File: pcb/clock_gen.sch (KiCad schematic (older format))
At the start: 0 parts

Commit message: schematic completed. Time for review
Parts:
- added C? (x2): 4.7u, symbol C
- added C? (x7): 0.47u, symbol C
- added FB? (x2): FILTER, symbol FILTER
- added U?: Si5338C, symbol Si5338C
- added U?: FOX924, symbol FOX924
- added U?: PL133-27, symbol PL133-27
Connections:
- net labels added: +3V3, CLK_GEN_IN, CLK_SCL, CLK_SDA, CLOCK_GEN_POWER, FPGA_CLK, GND, GTP_CLK_N, GTP_CLK_P, OSC_POWER, RF_CLK, RX_CLK, RX_CLK_FPGA, TX_CLK, TX_CLK_FPGA
- wire segments 0 -> 68

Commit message: Added part numbers and updated schematic
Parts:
- gave numbers to parts that had none: 14
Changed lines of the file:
@@
 $EndDescr
 $Comp
-L Si5338C U?
+L Si5338C U1003
 U 1 1 565F531B
 P 7600 2650
-F 0 "U?" H 7150 1750 60  0000 C CNN
+F 0 "U1003" H 7150 1750 60  0000 C CNN
 F 1 "Si5338C" H 7300 3550 60  0000 C CNN
 F 2 "" H 7400 2700 60  0000 C CNN
@@
 $EndComp
 $Comp
-L FOX924 U?
+L FOX924 U1001
 U 1 1 565F579F
 P 1900 1900
-F 0 "U?" H 1650 1550 60  0000 C CNN
+F 0 "U1001" H 1650 1550 60  0000 C CNN
 F 1 "FOX924" H 1750 2250 60  0000 C CNN
 F 2 "" H 1850 1800 60  0000 C CNN
@@
 $EndComp
 $Comp
-L PL133-27 U?
+L PL133-27 U1002
 U 1 1 565F5848
 P 3550 1850
-F 0 "U?" H 3350 1550 60  0000 C CNN
+F 0 "U1002" H 3350 1550 60  0000 C CNN
 F 1 "PL133-27" H 3550 2150 60  0000 C CNN
 F 2 "" H 3600 1700 60  0000 C CNN
@@
 $EndComp
 $Comp
-L GND #PWR?
+L GND #PWR1005
 U 1 1 565F599D
 P 3000 2300
-F 0 "#PWR?" H 3000 2050 50  0001 C CNN
+F 0 "#PWR1005" H 3000 2050 50  0001 C CNN
 F 1 "GND" H 3000 2150 50  0000 C CNN
 F 2 "" H 3000 2300 60  0000 C CNN
@@
 $EndComp
 $Comp
-L GND #PWR?
+L GND #PWR1001
 U 1 1 565F59BA
 P 1300 2300
-F 0 "#PWR?" H 1300 2050 50  0001 C CNN
+F 0 "#PWR1001" H 1300 2050 50  0001 C CNN
 F 1 "GND" H 1300 2150 50  0000 C CNN
 F 2 "" H 1300 2300 60  0000 C CNN
@@
 $EndComp
 $Comp
-L GND #PWR?
+L GND #PWR1009
 U 1 1 565F59F5
 P 6800 3500
-F 0 "#PWR?" H 6800 3250 50  0001 C CNN
+F 0 "#PWR1009" H 6800 3250 50  0001 C CNN
 F 1 "GND" H 6800 3350 50  0000 C CNN
 F 2 "" H 6800 3500 60  0000 C CNN
@@
 $EndComp
 $Comp
-L FILTER FB?
+L FILTER FB1002
 U 1 1 565F5A21
 P 2450 3700
-F 0 "FB?" H 2450 3850 50  0000 C CNN
+F 0 "FB1002" H 2450 3850 50  0000 C CNN
 F 1 "FILTER" H 2450 3600 50  0000 C CNN
 F 2 "" H 2450 3700 60  0000 C CNN
@@
 $EndComp
 $Comp
-L C C?
+L C C1002
 U 1 1 565F5A5C
 P 3000 3950
-F 0 "C?" H 3025 4050 50  0000 L CNN
+F 0 "C1002" H 3025 4050 50  0000 L CNN
 F 1 "4.7u" H 3025 3850 50  0000 L CNN
 F 2 "" H 3038 3800 30  0000 C CNN
@@
 $EndComp
 $Comp
-L C C?
+L C C1004
 U 1 1 565F5A91
 P 3300 3950
-F 0 "C?" H 3325 4050 50  0000 L CNN
+F 0 "C1004" H 3325 4050 50  0000 L CNN
 F 1 "0.47u" H 3325 3850 50  0000 L CNN
 F 2 "" H 3338 3800 30  0000 C CNN
@@
 $EndComp
 $Comp
-L C C?
+L C C1006
 U 1 1 565F5ABD
 P 3600 3950
-F 0 "C?" H 3625 4050 50  0000 L CNN
+F 0 "C1006" H 3625 4050 50  0000 L CNN
 F 1 "0.47u" H 3625 3850 50  0000 L CNN
 F 2 "" H 3638 3800 30  0000 C CNN
@@
 $EndComp
 $Comp
-L +3V3 #PWR?
+L +3V3 #PWR1003
 U 1 1 565F5B53
 P 2000 3600
-F 0 "#PWR?" H 2000 3450 50  0001 C CNN
+F 0 "#PWR1003" H 2000 3450 50  0001 C CNN
 F 1 "+3V3" H 2000 3740 50  0000 C CNN
 F 2 "" H 2000 3600 60  0000 C CNN
@@
 $EndComp
 $Comp
-L GND #PWR?
+L GND #PWR1006
 U 1 1 565F5C73
 P 3000 4300
-F 0 "#PWR?" H 3000 4050 50  0001 C CNN
+F 0 "#PWR1006" H 3000 4050 50  0001 C CNN
 F 1 "GND" H 3000 4150 50  0000 C CNN
 F 2 "" H 3000 4300 60  0000 C CNN
@@
 OSC_POWER
 $Comp
-L FILTER FB?
+L FILTER FB1001
 U 1 1 565F5D36
 P 2350 4800
-F 0 "FB?" H 2350 4950 50  0000 C CNN
+F 0 "FB1001" H 2350 4950 50  0000 C CNN
 F 1 "FILTER" H 2350 4700 50  0000 C CNN
 F 2 "" H 2350 4800 60  0000 C CNN
@@
 $EndComp
 $Comp
-L C C?
+L C C1001
 U 1 1 565F5D3C
 P 2900 5050
-F 0 "C?" H 2925 5150 50  0000 L CNN
+F 0 "C1001" H 2925 5150 50  0000 L CNN
 F 1 "4.7u" H 2925 4950 50  0000 L CNN
 F 2 "" H 2938 4900 30  0000 C CNN
@@
 $EndComp
 $Comp
-L C C?
+L C C1003
 U 1 1 565F5D42
 P 3200 5050
-F 0 "C?" H 3225 5150 50  0000 L CNN
+F 0 "C1003" H 3225 5150 50  0000 L CNN
 F 1 "0.47u" H 3225 4950 50  0000 L CNN
 F 2 "" H 3238 4900 30  0000 C CNN
@@
 $EndComp
 $Comp
-L C C?
+L C C1009
 U 1 1 565F5D48
 P 4300 5050
-F 0 "C?" H 4325 5150 50  0000 L CNN
+F 0 "C1009" H 4325 5150 50  0000 L CNN
 F 1 "0.47u" H 4325 4950 50  0000 L CNN
 F 2 "" H 4338 4900 30  0000 C CNN
@@
 $EndComp
 $Comp
-L +3V3 #PWR?
+L +3V3 #PWR1002
 U 1 1 565F5D4E
 P 1900 4700
-F 0 "#PWR?" H 1900 4550 50  0001 C CNN
+F 0 "#PWR1002" H 1900 4550 50  0001 C CNN
 F 1 "+3V3" H 1900 4840 50  0000 C CNN
 F 2 "" H 1900 4700 60  0000 C CNN
@@
 $EndComp
 $Comp
-L GND #PWR?
+L GND #PWR1004
 U 1 1 565F5D61
 P 2900 5400
-F 0 "#PWR?" H 2900 5150 50  0001 C CNN
+F 0 "#PWR1004" H 2900 5150 50  0001 C CNN
 F 1 "GND" H 2900 5250 50  0000 C CNN
 F 2 "" H 2900 5400 60  0000 C CNN
@@
 CLOCK_GEN_POWER
 $Comp
-L C C?
+L C C1005
 U 1 1 565F5DDA
 P 3500 5050
-F 0 "C?" H 3525 5150 50  0000 L CNN
+F 0 "C1005" H 3525 5150 50  0000 L CNN
 F 1 "0.47u" H 3525 4950 50  0000 L CNN
 F 2 "" H 3538 4900 30  0000 C CNN
@@
 $EndComp
 $Comp
-L C C?
+L C C1007
 U 1 1 565F5E43
 P 3800 5050
-F 0 "C?" H 3825 5150 50  0000 L CNN
+F 0 "C1007" H 3825 5150 50  0000 L CNN
 F 1 "0.47u" H 3825 4950 50  0000 L CNN
 F 2 "" H 3838 4900 30  0000 C CNN
@@
 $EndComp
 $Comp
-L C C?
+L C C1008
 U 1 1 565F607C
 P 4050 5050
-F 0 "C?" H 4075 5150 50  0000 L CNN
+F 0 "C1008" H 4075 5150 50  0000 L CNN
 F 1 "0.47u" H 4075 4950 50  0000 L CNN
 F 2 "" H 4088 4900 30  0000 C CNN
@@
 CLK_GEN_IN
 $Comp
-L GND #PWR?
+L GND #PWR1007
 U 1 1 565F65BD
 P 6500 2200
-F 0 "#PWR?" H 6500 1950 50  0001 C CNN
+F 0 "#PWR1007" H 6500 1950 50  0001 C CNN
 F 1 "GND" H 6500 2050 50  0000 C CNN
 F 2 "" H 6500 2200 60  0000 C CNN
@@
 CLK_GEN_IN
 $Comp
-L GND #PWR?
+L GND #PWR1008
 U 1 1 565F66BC
 P 6500 2600
-F 0 "#PWR?" H 6500 2350 50  0001 C CNN
+F 0 "#PWR1008" H 6500 2350 50  0001 C CNN
 F 1 "GND" H 6500 2450 50  0000 C CNN
 F 2 "" H 6500 2600 60  0000 C CNN

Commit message: mostly done with component placement
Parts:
- removed U1002: PL133-27, symbol PL133-27
- added U1002: NB3L553, wbraun_smd:DFN-8_2x2mm_Pitch0.5mm, symbol NB3L553
- C1001, C1002, C1003, C1004, C1005, C1006, C1007, C1008, C1009: footprint (none) -> wbraun_smd:C_0402
- FB1001, FB1002: footprint (none) -> wbraun_smd:L_0603
- U1001: footprint (none) -> wbraun_smd:OSCILLATOR_5.0X3.2
- U1003: footprint (none) -> wbraun_smd:QFN-24-1EP_4x4mm_Pitch0.5mm
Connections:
- wire segments 68 -> 69

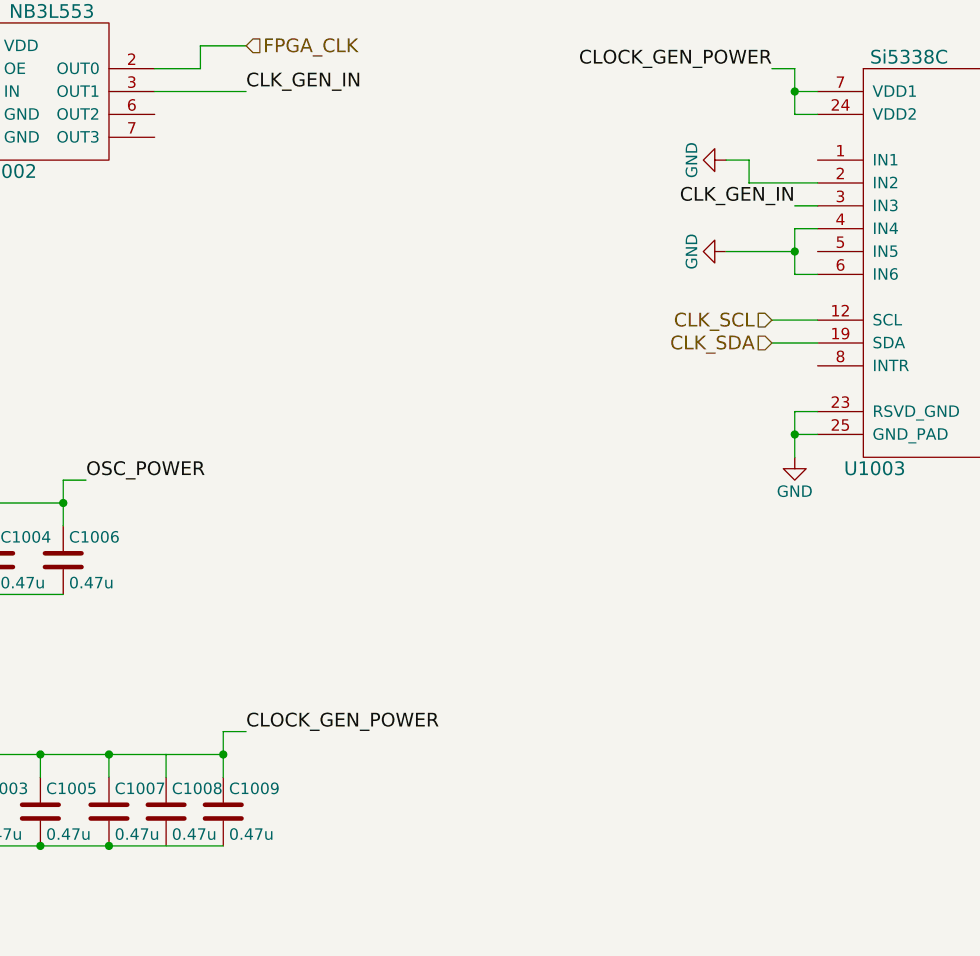
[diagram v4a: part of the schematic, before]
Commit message: Finished most of the routing, removed DDR-3
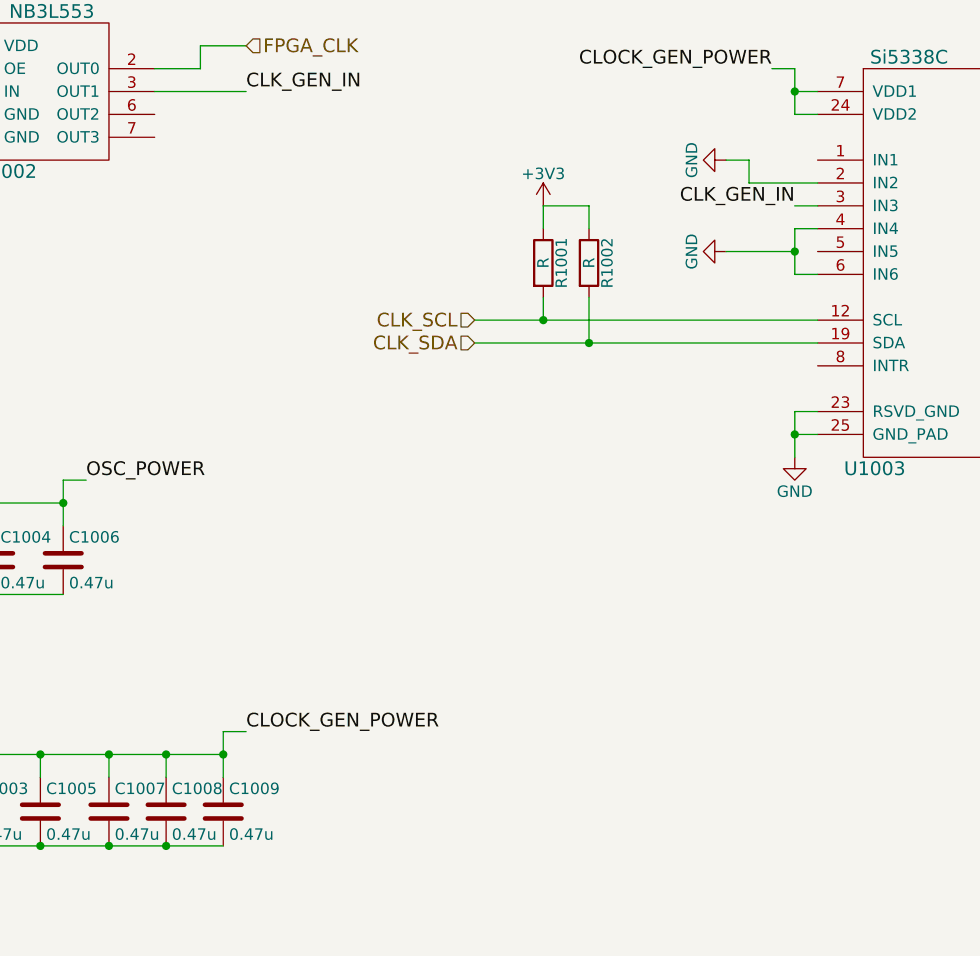
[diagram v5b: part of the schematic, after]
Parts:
- added R1001, R1002: R, wbraun_smd:R_0402, symbol R
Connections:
- net +3V3: now also R1001.1, R1002.1
- net CLK_SCL: now also R1001.2
- net CLK_SDA: now also R1002.2
- net CLOCK_GEN_POWER: now also C1008.1
- net GND: now also C1008.2
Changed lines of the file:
@@
 $Descr A4 11693 8268
 encoding utf-8
-Sheet 10 13
+Sheet 8 11
 Title ""
 Date ""
@@
 $EndComp
 $Comp
-L GND #PWR0144
+L GND #PWR0128
 U 1 1 565F599D
 P 3000 2300
-F 0 "#PWR0144" H 3000 2050 50  0001 C CNN
+F 0 "#PWR0128" H 3000 2050 50  0001 C CNN
 F 1 "GND" H 3000 2150 50  0000 C CNN
 F 2 "" H 3000 2300 60  0000 C CNN
@@
 $EndComp
 $Comp
-L GND #PWR0145
+L GND #PWR0129
 U 1 1 565F59BA
 P 1300 2300
-F 0 "#PWR0145" H 1300 2050 50  0001 C CNN
+F 0 "#PWR0129" H 1300 2050 50  0001 C CNN
 F 1 "GND" H 1300 2150 50  0000 C CNN
 F 2 "" H 1300 2300 60  0000 C CNN
@@
 $EndComp
 $Comp
-L GND #PWR0146
+L GND #PWR0130
 U 1 1 565F59F5
 P 6800 3500
-F 0 "#PWR0146" H 6800 3250 50  0001 C CNN
+F 0 "#PWR0130" H 6800 3250 50  0001 C CNN
 F 1 "GND" H 6800 3350 50  0000 C CNN
 F 2 "" H 6800 3500 60  0000 C CNN
@@
 $EndComp
 $Comp
-L +3V3 #PWR0147
+L +3V3 #PWR0131
 U 1 1 565F5B53
 P 2000 3600
-F 0 "#PWR0147" H 2000 3450 50  0001 C CNN
+F 0 "#PWR0131" H 2000 3450 50  0001 C CNN
 F 1 "+3V3" H 2000 3740 50  0000 C CNN
 F 2 "" H 2000 3600 60  0000 C CNN
@@
 $EndComp
 $Comp
-L GND #PWR0148
+L GND #PWR0132
 U 1 1 565F5C73
 P 3000 4300
-F 0 "#PWR0148" H 3000 4050 50  0001 C CNN
+F 0 "#PWR0132" H 3000 4050 50  0001 C CNN
 F 1 "GND" H 3000 4150 50  0000 C CNN
 F 2 "" H 3000 4300 60  0000 C CNN
@@
 $EndComp
 $Comp
-L +3V3 #PWR0149
+L +3V3 #PWR0133
 U 1 1 565F5D4E
 P 1900 4700
-F 0 "#PWR0149" H 1900 4550 50  0001 C CNN
+F 0 "#PWR0133" H 1900 4550 50  0001 C CNN
 F 1 "+3V3" H 1900 4840 50  0000 C CNN
 F 2 "" H 1900 4700 60  0000 C CNN
@@
 $EndComp
 $Comp
-L GND #PWR0150
+L GND #PWR0134
 U 1 1 565F5D61
 P 2900 5400
-F 0 "#PWR0150" H 2900 5150 50  0001 C CNN
+F 0 "#PWR0134" H 2900 5150 50  0001 C CNN
 F 1 "GND" H 2900 5250 50  0000 C CNN
 F 2 "" H 2900 5400 60  0000 C CNN
@@
 CLK_GEN_IN
 $Comp
-L GND #PWR0151
+L GND #PWR0135
 U 1 1 565F65BD
 P 6500 2200
-F 0 "#PWR0151" H 6500 1950 50  0001 C CNN
+F 0 "#PWR0135" H 6500 1950 50  0001 C CNN
 F 1 "GND" H 6500 2050 50  0000 C CNN
 F 2 "" H 6500 2200 60  0000 C CNN
@@
 CLK_GEN_IN
 $Comp
-L GND #PWR0152
+L GND #PWR0136
 U 1 1 565F66BC
 P 6500 2600
-F 0 "#PWR0152" H 6500 2350 50  0001 C CNN
+F 0 "#PWR0136" H 6500 2350 50  0001 C CNN
 F 1 "GND" H 6500 2450 50  0000 C CNN
 F 2 "" H 6500 2600 60  0000 C CNN
@@
 Text HLabel 8500 3300 2    60   Input ~ 0
 GTP_CLK_N
-Text HLabel 6700 2900 0    60   Input ~ 0
+Text HLabel 5400 2900 0    60   Input ~ 0
 CLK_SCL
-Text HLabel 6700 3000 0    60   Input ~ 0
+Text HLabel 5400 3000 0    60   Input ~ 0
 CLK_SDA
 Text HLabel 8500 2500 2    60   Input ~ 0
@@
 	8300 3300 8500 3300
 Wire Wire Line
-	6900 2900 6700 2900
-Wire Wire Line
-	6900 3000 6700 3000
+	5400 2900 6900 2900
+Wire Wire Line
+	5400 3000 6900 3000
 Wire Wire Line
 	3000 2000 3000 2300
@@
 Wire Wire Line
 	4400 1900 4000 1900
+$Comp
+L R R1001
+U 1 1 56672DC6
+P 5700 2650
+F 0 "R1001" V 5780 2650 50  0000 C CNN
+F 1 "R" V 5700 2650 50  0000 C CNN
+F 2 "wbraun_smd:R_0402" V 5630 2650 50  0001 C CNN
+F 3 "" H 5700 2650 50  0000 C CNN
+	1    5700 2650
+	1    0    0    -1
+$EndComp
+$Comp
+L R R1002
+U 1 1 56672EA0
+P 5900 2650
+F 0 "R1002" V 5980 2650 50  0000 C CNN
+F 1 "R" V 5900 2650 50  0000 C CNN
+F 2 "wbraun_smd:R_0402" V 5830 2650 50  0001 C CNN
+F 3 "" H 5900 2650 50  0000 C CNN
+	1    5900 2650
+	1    0    0    -1
+$EndComp
+Wire Wire Line
+	5700 2800 5700 2900
+Connection ~ 5700 2900
+Wire Wire Line
+	5900 2800 5900 3000
+Connection ~ 5900 3000
+$Comp
+L +3V3 #PWR0137
+U 1 1 5667326B
+P 5700 2400
+F 0 "#PWR0137" H 5700 2250 50  0001 C CNN
+F 1 "+3V3" H 5700 2540 50  0000 C CNN
+F 2 "" H 5700 2400 60  0000 C CNN
+F 3 "" H 5700 2400 60  0000 C CNN
+	1    5700 2400
+	1    0    0    -1
+$EndComp
+Wire Wire Line
+	5900 2500 5900 2400
+Wire Wire Line
+	5900 2400 5700 2400
+Wire Wire Line
+	5700 2400 5700 2500
+Connection ~ 4050 4800
+Connection ~ 4050 5200
 $EndSCHEMATC

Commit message: Pending final check
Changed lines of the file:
@@
 $EndComp
 $Comp
-L GND #PWR0128
+L GND #PWR0129
 U 1 1 565F599D
 P 3000 2300
-F 0 "#PWR0128" H 3000 2050 50  0001 C CNN
+F 0 "#PWR0129" H 3000 2050 50  0001 C CNN
 F 1 "GND" H 3000 2150 50  0000 C CNN
 F 2 "" H 3000 2300 60  0000 C CNN
@@
 $EndComp
 $Comp
-L GND #PWR0129
+L GND #PWR0130
 U 1 1 565F59BA
 P 1300 2300
-F 0 "#PWR0129" H 1300 2050 50  0001 C CNN
+F 0 "#PWR0130" H 1300 2050 50  0001 C CNN
 F 1 "GND" H 1300 2150 50  0000 C CNN
 F 2 "" H 1300 2300 60  0000 C CNN
@@
 $EndComp
 $Comp
-L GND #PWR0130
+L GND #PWR0131
 U 1 1 565F59F5
 P 6800 3500
-F 0 "#PWR0130" H 6800 3250 50  0001 C CNN
+F 0 "#PWR0131" H 6800 3250 50  0001 C CNN
 F 1 "GND" H 6800 3350 50  0000 C CNN
 F 2 "" H 6800 3500 60  0000 C CNN
@@
 $EndComp
 $Comp
-L +3V3 #PWR0131
+L +3V3 #PWR0132
 U 1 1 565F5B53
 P 2000 3600
-F 0 "#PWR0131" H 2000 3450 50  0001 C CNN
+F 0 "#PWR0132" H 2000 3450 50  0001 C CNN
 F 1 "+3V3" H 2000 3740 50  0000 C CNN
 F 2 "" H 2000 3600 60  0000 C CNN
@@
 $EndComp
 $Comp
-L GND #PWR0132
+L GND #PWR0133
 U 1 1 565F5C73
 P 3000 4300
-F 0 "#PWR0132" H 3000 4050 50  0001 C CNN
+F 0 "#PWR0133" H 3000 4050 50  0001 C CNN
 F 1 "GND" H 3000 4150 50  0000 C CNN
 F 2 "" H 3000 4300 60  0000 C CNN
@@
 $EndComp
 $Comp
-L +3V3 #PWR0133
+L +3V3 #PWR0134
 U 1 1 565F5D4E
 P 1900 4700
-F 0 "#PWR0133" H 1900 4550 50  0001 C CNN
+F 0 "#PWR0134" H 1900 4550 50  0001 C CNN
 F 1 "+3V3" H 1900 4840 50  0000 C CNN
 F 2 "" H 1900 4700 60  0000 C CNN
@@
 $EndComp
 $Comp
-L GND #PWR0134
+L GND #PWR0135
 U 1 1 565F5D61
 P 2900 5400
-F 0 "#PWR0134" H 2900 5150 50  0001 C CNN
+F 0 "#PWR0135" H 2900 5150 50  0001 C CNN
 F 1 "GND" H 2900 5250 50  0000 C CNN
 F 2 "" H 2900 5400 60  0000 C CNN
@@
 CLK_GEN_IN
 $Comp
-L GND #PWR0135
+L GND #PWR0136
 U 1 1 565F65BD
 P 6500 2200
-F 0 "#PWR0135" H 6500 1950 50  0001 C CNN
+F 0 "#PWR0136" H 6500 1950 50  0001 C CNN
 F 1 "GND" H 6500 2050 50  0000 C CNN
 F 2 "" H 6500 2200 60  0000 C CNN
@@
 CLK_GEN_IN
 $Comp
-L GND #PWR0136
+L GND #PWR0137
 U 1 1 565F66BC
 P 6500 2600
-F 0 "#PWR0136" H 6500 2350 50  0001 C CNN
+F 0 "#PWR0137" H 6500 2350 50  0001 C CNN
 F 1 "GND" H 6500 2450 50  0000 C CNN
 F 2 "" H 6500 2600 60  0000 C CNN
@@
 	8300 2000 8500 2000
 Wire Wire Line
-	8300 2100 8500 2100
-Wire Wire Line
 	8300 2400 8500 2400
 Wire Wire Line
@@
 Connection ~ 5900 3000
 $Comp
-L +3V3 #PWR0137
+L +3V3 #PWR0138
 U 1 1 5667326B
 P 5700 2400
-F 0 "#PWR0137" H 5700 2250 50  0001 C CNN
+F 0 "#PWR0138" H 5700 2250 50  0001 C CNN
 F 1 "+3V3" H 5700 2540 50  0000 C CNN
 F 2 "" H 5700 2400 60  0000 C CNN
